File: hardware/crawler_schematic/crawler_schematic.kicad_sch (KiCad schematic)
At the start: 12 parts, among them J1 Conn_01x02_Pin, J2 MP1584 Buck Converter, M1 Motor_DC, M2 Motor_Servo, U1 NRF24L01

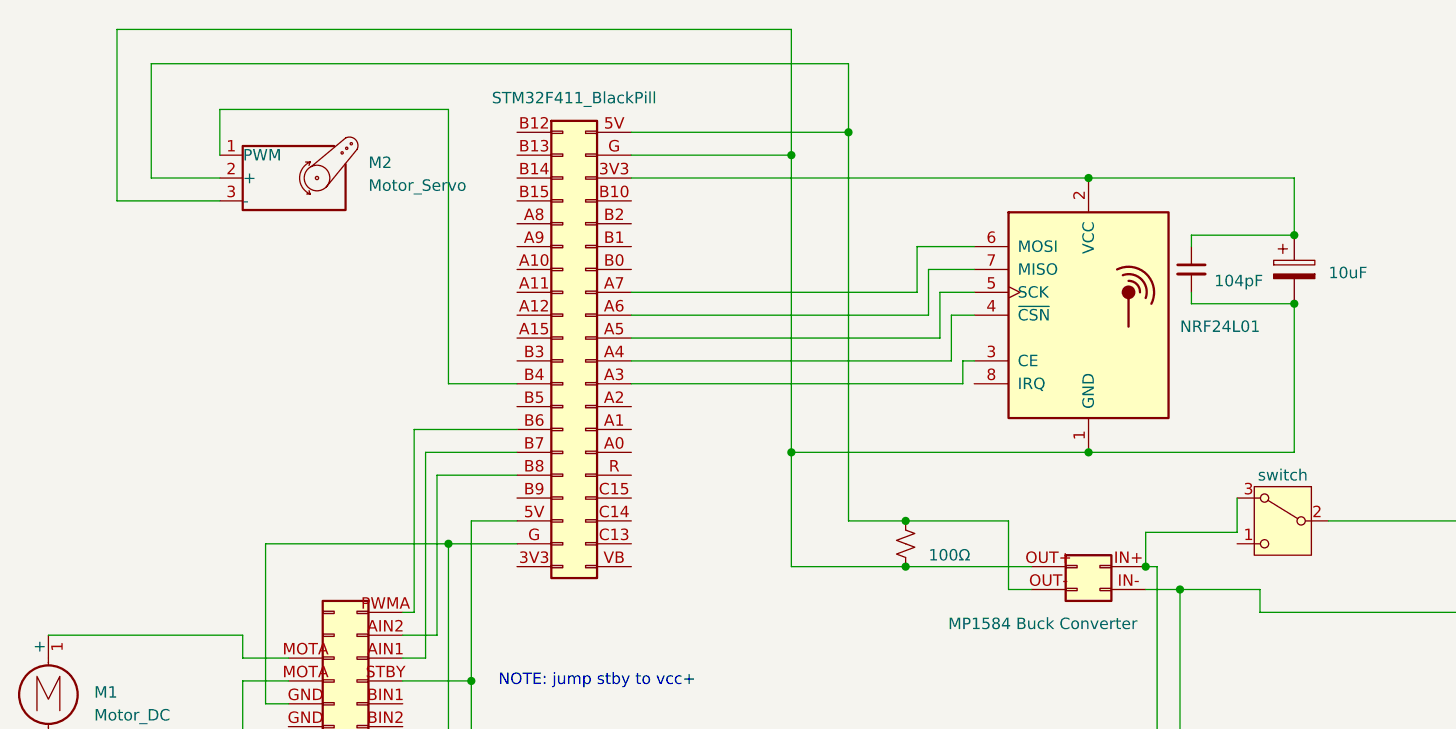
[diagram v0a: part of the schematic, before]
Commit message: fix: 5V/Gnd schema for servo and buck
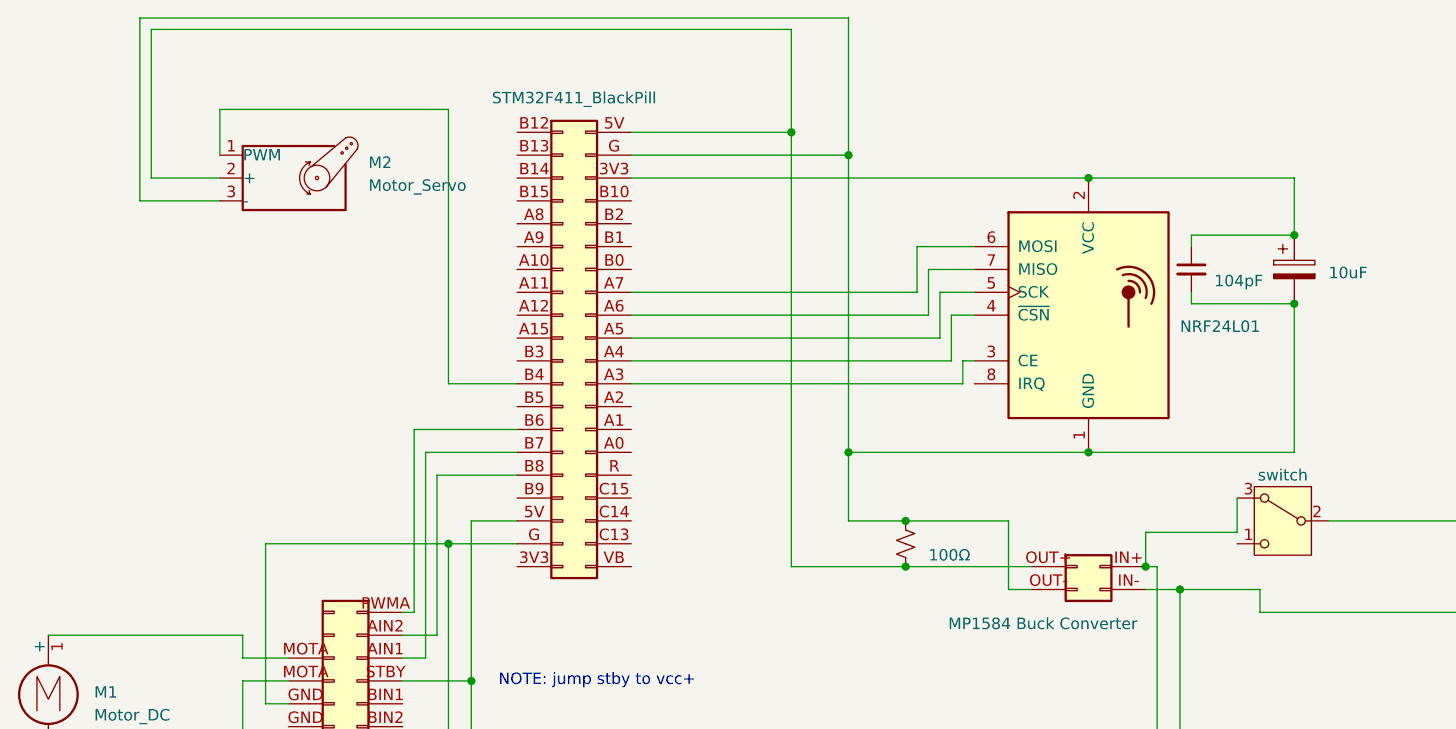
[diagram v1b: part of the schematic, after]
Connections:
- net at TB6612_HBridge.GND (Pin_15): now also STM32F411_BlackPill.G (Pin_39)
- net at STM32F411_BlackPill.G (Pin_39): now also C1.2, C2.2, J2.OUT- (Pin_2), M2.3 (-), R1.1, U1.1 (GND); no longer TB6612_HBridge.GND (Pin_15)
- net at M2.2 (+), STM32F411_BlackPill.5V (Pin_40): now also J2.OUT+ (Pin_1), R1.2; no longer J2.OUT- (Pin_2), R1.1
- net at STM32F411_BlackPill.3V3 (Pin_38): now also C1.1, C2.1, U1.2 (VCC)
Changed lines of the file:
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@@
-	)
-	(junction
-		(at 109.22 67.31)
-		(diameter 0)
-		(color 0 0 0 0)
-	)
-	(junction
-		(at 115.57 31.75)
-		(diameter 0)
-		(color 0 0 0 0)
 	)
 	(junction
@@
 	)
 	(junction
+		(at 142.24 67.31)
+		(diameter 0)
+		(color 0 0 0 0)
+	)
+	(junction
+		(at 115.57 67.31)
+		(diameter 0)
+		(color 0 0 0 0)
+	)
+	(junction
 		(at 152.4 82.55)
 		(diameter 0)
@@
 	)
 	(junction
-		(at 142.24 67.31)
-		(diameter 0)
-		(color 0 0 0 0)
-	)
-	(junction
-		(at 109.22 34.29)
+		(at 115.57 34.29)
+		(diameter 0)
+		(color 0 0 0 0)
+	)
+	(junction
+		(at 109.22 31.75)
 		(diameter 0)
 		(color 0 0 0 0)
@@
 	(wire
 		(pts
-			(xy 115.57 24.13) (xy 115.57 31.75)
-		)
-		(stroke
-			(width 0)
-			(type default)
-		)
-	)
-	(wire
-		(pts
 			(xy 66.04 85.09) (xy 67.31 85.09)
 		)
@@
 	(wire
 		(pts
-			(xy 109.22 67.31) (xy 142.24 67.31)
-		)
-		(stroke
-			(width 0)
-			(type default)
-		)
-	)
-	(wire
-		(pts
 			(xy 71.12 77.47) (xy 78.74 77.47)
 		)
@@
 	(wire
 		(pts
-			(xy 91.44 34.29) (xy 109.22 34.29)
-		)
-		(stroke
-			(width 0)
-			(type default)
-		)
-	)
-	(wire
-		(pts
 			(xy 71.12 59.69) (xy 78.74 59.69)
 		)
@@
 	(wire
 		(pts
-			(xy 34.29 20.32) (xy 109.22 20.32)
-		)
-		(stroke
-			(width 0)
-			(type default)
-		)
-	)
-	(wire
-		(pts
-			(xy 115.57 31.75) (xy 115.57 74.93)
-		)
-		(stroke
-			(width 0)
-			(type default)
-		)
-	)
-	(wire
-		(pts
 			(xy 50.8 95.25) (xy 50.8 77.47)
 		)
@@
 	(wire
 		(pts
+			(xy 115.57 67.31) (xy 115.57 74.93)
+		)
+		(stroke
+			(width 0)
+			(type default)
+		)
+	)
+	(wire
+		(pts
 			(xy 91.44 52.07) (xy 124.46 52.07)
 		)
@@
 	(wire
 		(pts
+			(xy 38.1 20.32) (xy 38.1 36.83)
+		)
+		(stroke
+			(width 0)
+			(type default)
+		)
+	)
+	(wire
+		(pts
 			(xy 68.58 67.31) (xy 78.74 67.31)
 		)
@@
 	(wire
 		(pts
+			(xy 36.83 19.05) (xy 36.83 39.37)
+		)
+		(stroke
+			(width 0)
+			(type default)
+		)
+	)
+	(wire
+		(pts
 			(xy 149.86 111.76) (xy 149.86 80.01)
 		)
@@
 	(wire
 		(pts
-			(xy 165.1 67.31) (xy 142.24 67.31)
+			(xy 115.57 34.29) (xy 115.57 67.31)
 		)
 		(stroke
@@
 	(wire
 		(pts
-			(xy 34.29 39.37) (xy 34.29 20.32)
+			(xy 91.44 34.29) (xy 115.57 34.29)
 		)
 		(stroke
@@
 	(wire
 		(pts
-			(xy 109.22 34.29) (xy 109.22 67.31)
+			(xy 109.22 20.32) (xy 109.22 31.75)
 		)
 		(stroke
@@
 	(wire
 		(pts
-			(xy 91.44 31.75) (xy 115.57 31.75)
-		)
-		(stroke
-			(width 0)
-			(type default)
-		)
-	)
-	(wire
-		(pts
-			(xy 38.1 36.83) (xy 38.1 24.13)
-		)
-		(stroke
-			(width 0)
-			(type default)
-		)
-	)
-	(wire
-		(pts
 			(xy 121.92 80.01) (xy 135.89 80.01)
 		)
@@
 	(wire
 		(pts
-			(xy 38.1 24.13) (xy 115.57 24.13)
+			(xy 142.24 67.31) (xy 165.1 67.31)
 		)
 		(stroke
@@
 	(wire
 		(pts
+			(xy 115.57 67.31) (xy 142.24 67.31)
+		)
+		(stroke
+			(width 0)
+			(type default)
+		)
+	)
+	(wire
+		(pts
 			(xy 153.67 43.18) (xy 165.1 43.18)
 		)
@@
 	(wire
 		(pts
-			(xy 109.22 20.32) (xy 109.22 34.29)
+			(xy 36.83 39.37) (xy 45.72 39.37)
 		)
 		(stroke
@@
 	(wire
 		(pts
+			(xy 109.22 20.32) (xy 38.1 20.32)
+		)
+		(stroke
+			(width 0)
+			(type default)
+		)
+	)
+	(wire
+		(pts
 			(xy 158.75 76.2) (xy 148.59 76.2)
 		)
@@
 	(wire
 		(pts
-			(xy 45.72 36.83) (xy 38.1 36.83)
-		)
-		(stroke
-			(width 0)
-			(type default)
-		)
-	)
-	(wire
-		(pts
-			(xy 109.22 67.31) (xy 109.22 80.01)
+			(xy 109.22 31.75) (xy 109.22 80.01)
 		)
 		(stroke
@@
 	(wire
 		(pts
-			(xy 45.72 39.37) (xy 34.29 39.37)
+			(xy 115.57 19.05) (xy 36.83 19.05)
 		)
 		(stroke
@@
 	(wire
 		(pts
+			(xy 91.44 31.75) (xy 109.22 31.75)
+		)
+		(stroke
+			(width 0)
+			(type default)
+		)
+	)
+	(wire
+		(pts
 			(xy 91.44 54.61) (xy 125.73 54.61)
 		)
@@
 	(wire
 		(pts
+			(xy 115.57 19.05) (xy 115.57 34.29)
+		)
+		(stroke
+			(width 0)
+			(type default)
+		)
+	)
+	(wire
+		(pts
 			(xy 66.04 105.41) (xy 73.66 105.41)
 		)
@@
 		)
 		(stroke
+			(width 0)
+			(type default)
+		)
+	)
+	(wire
+		(pts
+			(xy 38.1 36.83) (xy 45.72 36.83)
+		)
+		(stroke

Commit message: update: schematic cleanup for pcb_r1
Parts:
- removed 2S_Lipo: 2S Lipo, symbol Device:Battery
- removed J2: MP1584 Buck Converter, symbol Connector_Generic:Conn_02x02_Counter_Clockwise
- removed R1: 100Ω, symbol Device:R_Small_US
- removed SW?: switch, Button_Switch_SMD:Nidec_Copal_CAS-120A, symbol Switch:SW_Nidec_CAS-120A1
- renumbered STM32F411_BlackPill to STM32F411, TB6612_HBridge to TB6612
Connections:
- net GND: now reaches TB6612.GND (Pin_15)
- net GND: now also C1.2, C2.2, J1.VMoT- (Pin_2), M2.3 (-), STM32F411.G (Pin_39), U1.1 (GND)
- net at M1.1 (+): now also TB6612.+MOTA (Pin_13); no longer TB6612.MOTA (Pin_13)
- net at M1.2 (-): now also TB6612.-MOTA (Pin_14); no longer TB6612.MOTA (Pin_13)
- net +5V: now reaches STM32F411.5V (Pin_40), TB6612.STBY (Pin_7), TB6612.VCC (Pin_2)
- net +5V: now also M2.2 (+)
- net +BATT: now reaches J1.VMot+ (Pin_1)
- net bp_3v3: now reaches STM32F411.3V3 (Pin_38)
- net +3.3V: now reaches C1.1, C2.1, U1.2 (VCC)
- net +3.3V: no longer STM32F411.3V3 (Pin_38)
- net at STM32F411.A3 (Pin_29): now also U1.8 (IRQ); no longer U1.3 (CE)
- no-connect marks 0 -> 32
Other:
- added sheet Power Sheet (power.kicad_sch)
- moved on the sheet: M1, M2, TB6612

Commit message: update: schematic complete, start pcb design
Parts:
- removed J1: Conn_01x02_Pin, symbol Connector:Conn_01x02_Pin
- removed M1: Motor_DC, symbol Motor:Motor_DC
- removed TB6612: Conn_02x10_Counter_Clockwise, symbol Connector_Generic:Conn_02x10_Counter_Clockwise
- added C3, C4: 10uF, Capacitor_SMD:C_1206_3216Metric, symbol Device:C_Small
- added J4: JST-PH, Connector_JST:JST_PH_S2B-PH-K_1x02_P2.00mm_Horizontal, symbol Connector:Conn_01x02_Pin
- added R1: 10k Ohm, Resistor_SMD:R_0201_0603Metric, symbol Device:R_Small_US
- added U2: TB6612FNG, Package_SO:SSOP-24_5.3x8.2mm_P0.65mm, symbol Driver_Motor:TB6612FNG
- C1: footprint (none) -> Capacitor_SMD:C_1206_3216Metric
- C2: value 104pF -> 104nF; footprint (none) -> Capacitor_SMD:C_1206_3216Metric
- M2: footprint (none) -> Connector_PinHeader_2.54mm:PinHeader_1x03_P2.54mm_Vertical
- STM32F411: footprint (none) -> Package_DIP:DIP-40_W15.24mm_Socket
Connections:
- net +5V: now also C3.1, R1.1, U2.20 (VCC)
- net +BATT: now also C4.1, U2.13 (VM2), U2.14 (VM3), U2.24 (VM1)
- net GND: now also C3.2, C4.2, U2.10 (PGND2), U2.18 (GND), U2.3 (PGND1), U2.4 (PGND1), U2.9 (PGND2)
- net at STM32F411.B7 (Pin_15): now also U2.21 (AIN1)
- net at STM32F411.B8 (Pin_16): now also U2.22 (AIN2)
- net at STM32F411.B6 (Pin_14): now also U2.23 (PWMA)
- new net: J4.1 (Pin_1), U2.1 (AO1), U2.2 (AO1)
- new net: J4.2 (Pin_2), U2.5 (AO2), U2.6 (AO2)
- new net: R1.2, U2.19 (STBY)
- new net: U2.11 (BO1), U2.12 (BO1)
- new net: U2.7 (BO2), U2.8 (BO2)
- no-connect marks 32 -> 31
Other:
- note removed: "NOTE: jump stby to vcc+"

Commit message: update: revamp crawler schematic
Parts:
- removed C1: 10uF, Capacitor_SMD:C_1206_3216Metric, symbol Device:C_Polarized
- removed C2: 104nF, Capacitor_SMD:C_1206_3216Metric, symbol Device:C_Small
- removed C3, C4: 10uF, Capacitor_SMD:C_1206_3216Metric, symbol Device:C_Small
- removed J4: JST-PH, Connector_JST:JST_PH_S2B-PH-K_1x02_P2.00mm_Horizontal, symbol Connector:Conn_01x02_Pin
- removed R1: 10k Ohm, Resistor_SMD:R_0201_0603Metric, symbol Device:R_Small_US
- removed STM32F411: STM32F411_BlackPill, Package_DIP:DIP-40_W15.24mm_Socket, symbol Connector_Generic:Conn_02x20_Counter_Clockwise
- removed U1: NRF24L01, RF_Module:nRF24L01_Breakout, symbol RF:NRF24L01_Breakout
- added C1_3.?, C1_?: 100nF, Capacitor_SMD:C_1206_3216Metric, symbol Device:C_Small
- added C? (x2): 10uF, Capacitor_SMD:C_1206_3216Metric, symbol Device:C_Small
- added C?: 104nF, Capacitor_SMD:C_1206_3216Metric, symbol Device:C_Small
- added C?: 10uF, Capacitor_SMD:C_1206_3216Metric, symbol Device:C_Polarized
- added CFF_3.?, CFF_?: Opt., Capacitor_SMD:C_1206_3216Metric, symbol Device:C_Small
- added CIN_3.?, CIN_?: 22uF, Capacitor_SMD:C_1206_3216Metric, symbol Device:C_Polarized
- added COUT_3.?, COUT_?: 22x2uF, Capacitor_SMD:C_1206_3216Metric, symbol Device:C_Polarized
- added J1 (x2): JST-PH, Connector_JST:JST_PH_S2B-PH-K_1x02_P2.00mm_Horizontal, symbol Connector:Conn_01x02_Pin
- added J3: SWD_Header, Package_DFN_QFN:WDFN-10-1EP_3x3mm_P0.5mm_EP1.8x2.5mm, symbol Connector_Generic:Conn_01x04
- added L1_3.?, L1_?: 4.7uH, Inductor_SMD:L_Cenker_CKCS8040, symbol Device:L_Small
- added Q?: AO4407A, easyeda2kicad:SOIC-8_L4.9-W3.9-P1.27-LS6.0-BL, symbol RY8336:AO4407A
- added R1_3.?: 25.68 kOhm, Resistor_SMD:R_0201_0603Metric, symbol Device:R_Small_US
- added R1_?: 44.05 kOhm, Resistor_SMD:R_0201_0603Metric, symbol Device:R_Small_US
- added R2_3.?, R2_?, R?, R_EN_3.?, R_EN_?: 10 kOhm, Resistor_SMD:R_0201_0603Metric, symbol Device:R_Small_US
- added R?: 10k Ohm, Resistor_SMD:R_0201_0603Metric, symbol Device:R_Small_US
- added U1: STM32F411CEUx, Package_DFN_QFN:QFN-48-1EP_7x7mm_P0.5mm_EP5.6x5.6mm, symbol MCU_ST_STM32F4:STM32F411CEUx
- added U?: NRF24L01, RF_Module:nRF24L01_Breakout, symbol RF:NRF24L01_Breakout
- added U?, U_3.?: RY8336, easyeda2kicad:ESOP-8_L4.9-W3.9-P1.27-LS6.0-BL-EP-1, symbol RY8336:RY8336
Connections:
- net +3.3V: now also C?.1, C?.1, CFF_3.?.1, COUT_3.?.1, J3.1 (Pin_1), L1_3.?.2, R1_3.?.2, U?.2 (VCC)
- net +5V: now also C?.1, CFF_?.1, COUT_?.1, L1_?.2, R1_?.2, R?.1; no longer M2.2 (+)
- net +BATT: now also C?.1, CIN_3.?.1, CIN_?.1, Q?.1 (S), Q?.2 (S), Q?.3 (S), R_EN_3.?.2, R_EN_?.2, U?.2 (IN), U_3.?.2 (IN)
- net GND: now also C?.2, C?.2, C?.2, C?.2, CIN_3.?.2, CIN_?.2, COUT_3.?.2, COUT_?.2, J1.2 (Pin_2), J3.4 (Pin_4), R2_3.?.1, R2_?.1, R?.1, U?.1 (GND), U?.4 (GND), U?.9 (GND), U_3.?.4 (GND), U_3.?.9 (GND); no longer M2.3 (-)
- net servo_pwm: now reaches M2.1 (servo_pwm)
- net servo_pwm: now also U1.40 (PB4)
- net PWMA: now reaches U2.23 (PWMA)
- net PWMA: now also U1.42 (PB6)
- net AIN1: now reaches U2.21 (AIN1)
- net AIN1: now also U1.43 (PB7)
- net AIN2: now reaches U2.22 (AIN2)
- net AIN2: now also U1.45 (PB8)
- net AO1: now reaches U2.1 (AO1), U2.2 (AO1)
- net AO1: now also J1.1 (Pin_1)
- net AO2: now reaches U2.5 (AO2), U2.6 (AO2)
- net AO2: now also J1.2 (Pin_2)
- net at U2.19 (STBY): now also R?.2
- new net: C1_3.?.2, L1_3.?.1, U_3.?.3 (SW)
- new net: CFF_?.2, R1_?.1, R2_?.2, U?.5 (FB)
- new net: C1_3.?.1, U_3.?.1 (BS)
- new net: R_EN_?.1, U?.7 (EN)
- new net: C1_?.2, L1_?.1, U?.3 (SW)
- new net: CFF_3.?.2, R1_3.?.1, R2_3.?.2, U_3.?.5 (FB)
- new net: U1.23 (VSS), U1.35 (VSS), U1.47 (VSS), U1.49 (VSS)
- new net: C1_?.1, U?.1 (BS)
- new net: Q?.4 (G), R?.2
- new net: J1.1 (Pin_1), Q?.5 (D), Q?.6 (D), Q?.7 (D), Q?.8 (D)
- new net: R_EN_3.?.1, U_3.?.7 (EN)
- new net IRQ: U1.13 (PA3), U?.8 (IRQ)
- new net MISO: U1.16 (PA6), U?.7 (MISO)
- new net MOSI: U1.17 (PA7), U?.6 (MOSI)
- new net PA13: J3.2 (Pin_2), U1.34 (PA13)
- new net PA14: J3.3 (Pin_3), U1.37 (PA14)
- new net SCK: U1.15 (PA5), U?.5 (SCK)
- new net ~{CSN}: U1.14 (PA4), U?.4 (~{CSN})
- no-connect marks 31 -> 10
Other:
- added sheet stm32f411ce (stm32f411ce.kicad_sch)

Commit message: fix: CSN going high too early caused 4 byte corruption, CRC blocked RX. Delay added to chip_deselect in nrf driver, not full solution
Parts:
- gave numbers to parts that had none: 2
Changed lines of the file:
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@@
 		(dnp no)
 		(fields_autoplaced yes)
-		(property "Reference" "U?"
+		(property "Reference" "U2"
 			(at 109.22 34.29 0)
 			(show_name no)
@@
 			(project "crawler_schematic"
 				(path "/c2149483-af64-427b-b729-f25068fe8a40"
-					(reference "U?")
+					(reference "U2")
 					(unit 1)
 				)
@@
 		(dnp no)
 		(fields_autoplaced yes)
-		(property "Reference" "U_3.?"
+		(property "Reference" "U3"
 			(at 110.49 77.47 0)
 			(show_name no)
@@
 			(project "crawler_schematic"
 				(path "/c2149483-af64-427b-b729-f25068fe8a40"
-					(reference "U_3.?")
-					(unit 1)
-				)
+					(reference "U3")
+					(unit 1)
+				)
